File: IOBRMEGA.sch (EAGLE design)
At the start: 21 parts, among them J1 Digital_0_7, J10 Power, J2 Analog, J3 Digital_8_13, J4 Analog, J5 Digital_0_7, J6 Digital_22_36, J7 Digital_23_37, J8 Digital_38_52, J9 Digital_39_53

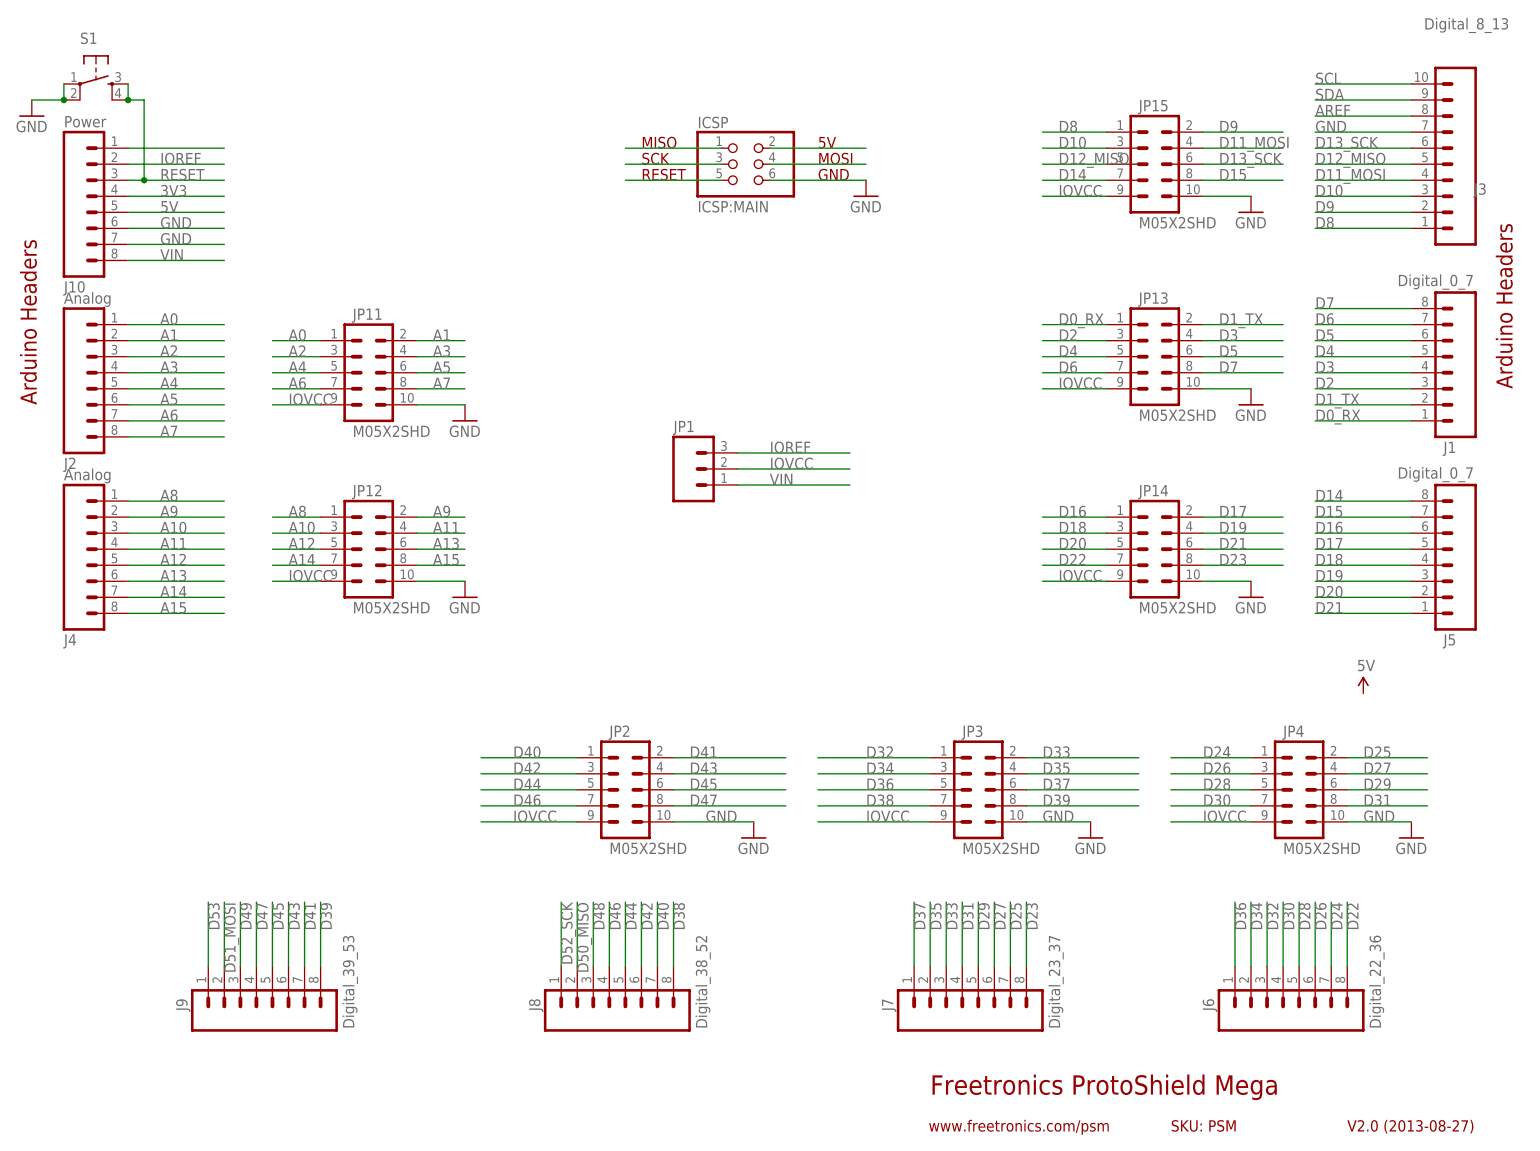
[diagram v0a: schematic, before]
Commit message: Expanded headers to 2x6 to include IOREF and RESET for v2.0 release
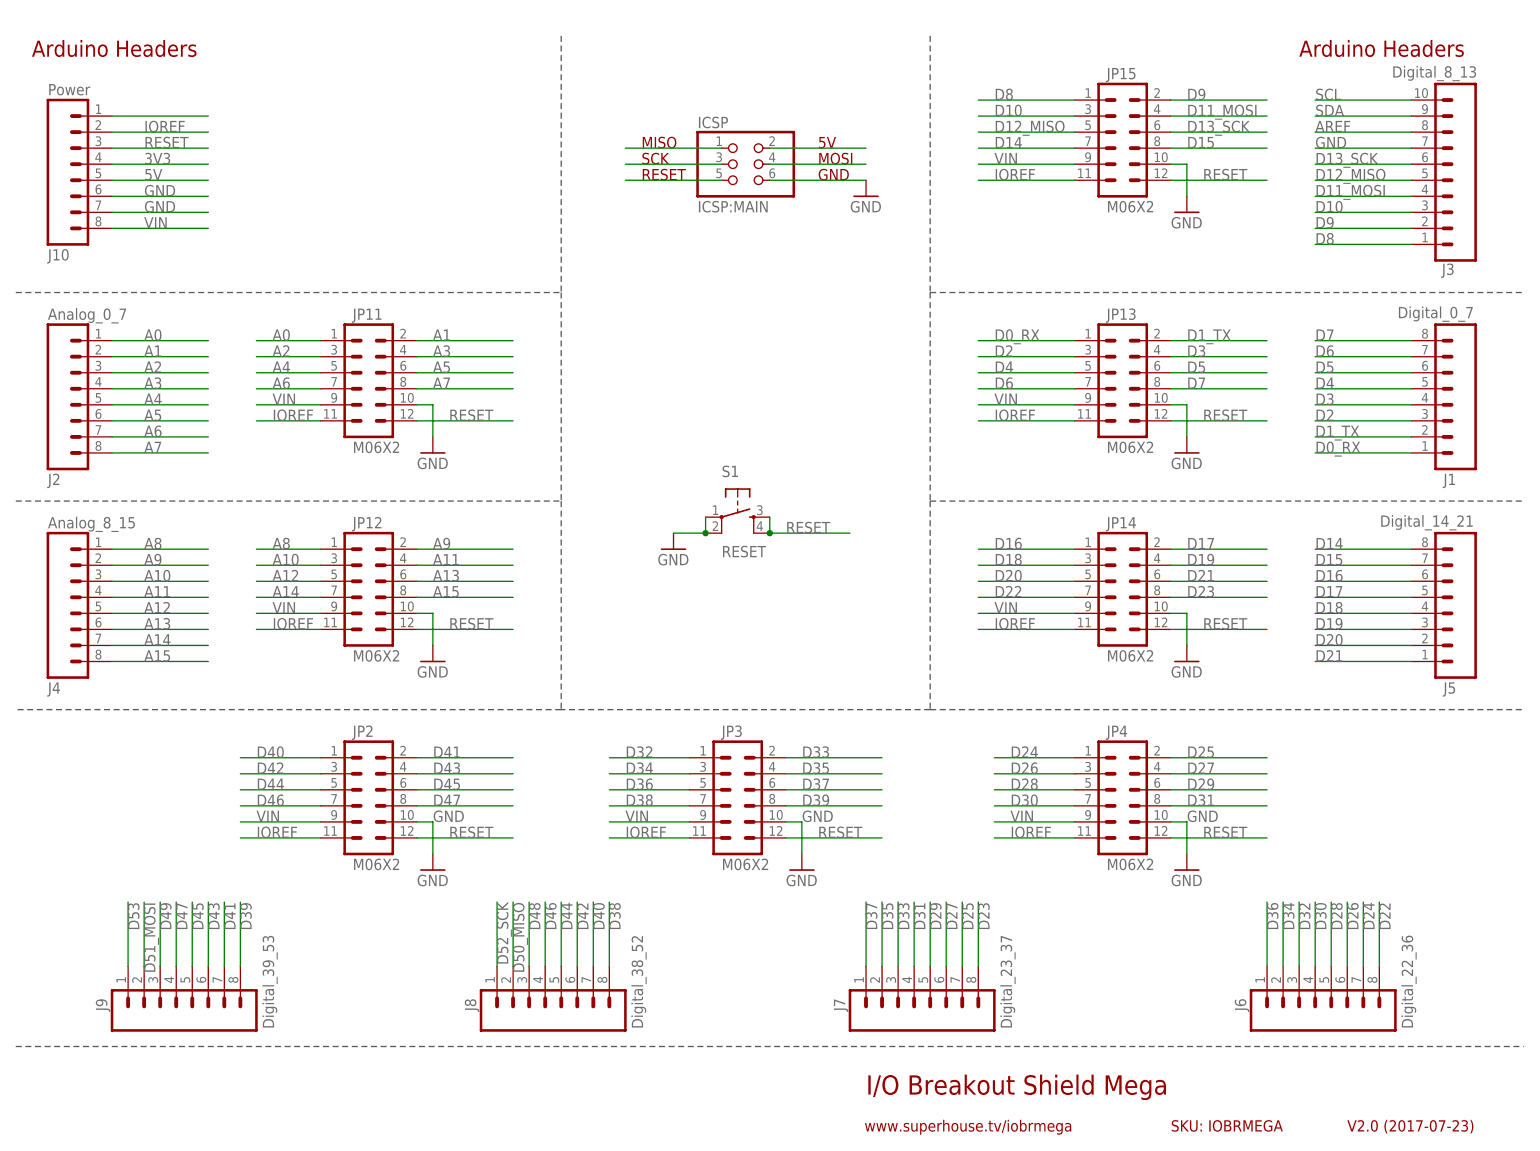
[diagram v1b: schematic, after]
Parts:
- removed JP1: (no value), freetronics-master-v1.1:M03PTH
- J2: value Analog -> Analog_0_7
- J4: value Analog -> Analog_8_15
- J5: value Digital_0_7 -> Digital_14_21
- JP11, JP12, JP13, JP14, JP15, JP2, JP3, JP4: value M05X2SHD -> M06X2; device freetronics-original:M05X2SHD -> freetronics-jon:M06X2
- S1: value (none) -> RESET
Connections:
- removed net IOVCC: JP1.2, JP11.9, JP12.9, JP13.9, JP14.9, JP15.9, JP2.9, JP3.9, JP4.9
- net IOREF: now also JP11.11, JP12.11, JP13.11, JP14.11, JP15.11, JP2.11, JP3.11, JP4.11; no longer JP1.3
- net RESET: now also JP11.12, JP12.12, JP13.12, JP14.12, JP15.12, JP2.12, JP3.12, JP4.12
- net VIN: now also JP11.9, JP12.9, JP13.9, JP14.9, JP15.9, JP2.9, JP3.9, JP4.9; no longer JP1.1
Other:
- note added: "I/O Breakout Shield Mega"
- note added: "SKU: IOBRMEGA"
- note added: "V2.0 (2017-07-23)"
- note added: "www.superhouse.tv/iobrmega"
- note removed: "Freetronics ProtoShield Mega"
- note removed: "SKU: PSM"
- note removed: "V2.0 (2013-08-27)"
- note removed: "www.freetronics.com/psm"
- moved on the sheet: J1, J10, J2, J3, J4, J5, J6, J7, J8, J9, S1

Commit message: Part swap to SuperHouse library to add 3D models
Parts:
- JP11, JP12, JP13, JP14, JP15, JP2, JP3, JP4: value M06X2 -> M06X2-SHROUDED; device freetronics-jon:M06X2 -> SuperHouse-Connectors:M06X2-SHROUDED
- S1: device freetronics-master-v1:TAC_SWITCHPTH -> SuperHouse-Switches:TAC_SWITCH-PTH-6

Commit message: Updated for v2.1 release
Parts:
- J1, J5, J6, J7, J8, J9: device freetronics:M08 -> SuperHouse-Connectors:M08-PIN-BELOW
- J10, J2, J4: device freetronics-master-v1:M08 -> SuperHouse-Connectors:M08-PIN-BELOW
- J3: device freetronics-original:M100.1 -> SuperHouse-Connectors:M10-PIN-BELOW
- renumbered ICSP to J19, JP11 to J11, JP12 to J12, JP13 to J17, JP14 to J16, JP15 to J18, JP2 to J13, JP3 to J14, JP4 to J15
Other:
- note added: "V2.1 (2019-10-25)"
- note removed: "V2.0 (2017-07-23)"

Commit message: Final tweaks for v2.1 release
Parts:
- J11, J12, J13, J14, J15, J16, J17, J18: value M06X2-SHROUDED -> M02X6-SHROUDED; device SuperHouse-Connectors:M06X2-SHROUDED -> SuperHouse-Connectors:M02X6-SHROUDED
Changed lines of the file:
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@@
 <part name="J8" library="SuperHouse-Connectors" library_urn="urn:adsk.eagle:library:11765989" deviceset="M08" device="-PIN-BELOW" package3d_urn="urn:adsk.eagle:package:14732715/3" value="Digital_38_52"/>
 <part name="J9" library="SuperHouse-Connectors" library_urn="urn:adsk.eagle:library:11765989" deviceset="M08" device="-PIN-BELOW" package3d_urn="urn:adsk.eagle:package:14732715/3" value="Digital_39_53"/>
-<part name="J19" library="pinhead" deviceset="PINHD-2X3" device="" value="ICSP:MAIN"/>
+<part name="J19" library="pinhead" library_urn="urn:adsk.eagle:library:325" deviceset="PINHD-2X3" device="" package3d_urn="urn:adsk.eagle:package:22462/2" value="ICSP:MAIN"/>
 <part name="J10" library="SuperHouse-Connectors" library_urn="urn:adsk.eagle:library:11765989" deviceset="M08" device="-PIN-BELOW" package3d_urn="urn:adsk.eagle:package:14732715/3" value="Power"/>
-<part name="J11" library="SuperHouse-Connectors" library_urn="urn:adsk.eagle:library:11765989" deviceset="M06X2" device="-SHROUDED" package3d_urn="urn:adsk.eagle:package:11976015/2"/>
-<part name="J12" library="SuperHouse-Connectors" library_urn="urn:adsk.eagle:library:11765989" deviceset="M06X2" device="-SHROUDED" package3d_urn="urn:adsk.eagle:package:11976015/2"/>
-<part name="J17" library="SuperHouse-Connectors" library_urn="urn:adsk.eagle:library:11765989" deviceset="M06X2" device="-SHROUDED" package3d_urn="urn:adsk.eagle:package:11976015/2"/>
-<part name="J16" library="SuperHouse-Connectors" library_urn="urn:adsk.eagle:library:11765989" deviceset="M06X2" device="-SHROUDED" package3d_urn="urn:adsk.eagle:package:11976015/2"/>
-<part name="J18" library="SuperHouse-Connectors" library_urn="urn:adsk.eagle:library:11765989" deviceset="M06X2" device="-SHROUDED" package3d_urn="urn:adsk.eagle:package:11976015/2"/>
-<part name="J13" library="SuperHouse-Connectors" library_urn="urn:adsk.eagle:library:11765989" deviceset="M06X2" device="-SHROUDED" package3d_urn="urn:adsk.eagle:package:11976015/2"/>
-<part name="J14" library="SuperHouse-Connectors" library_urn="urn:adsk.eagle:library:11765989" deviceset="M06X2" device="-SHROUDED" package3d_urn="urn:adsk.eagle:package:11976015/2"/>
-<part name="J15" library="SuperHouse-Connectors" library_urn="urn:adsk.eagle:library:11765989" deviceset="M06X2" device="-SHROUDED" package3d_urn="urn:adsk.eagle:package:11976015/2"/>
+<part name="J11" library="SuperHouse-Connectors" library_urn="urn:adsk.eagle:library:11765989" deviceset="M02X6" device="-SHROUDED" package3d_urn="urn:adsk.eagle:package:11976015/5"/>
+<part name="J12" library="SuperHouse-Connectors" library_urn="urn:adsk.eagle:library:11765989" deviceset="M02X6" device="-SHROUDED" package3d_urn="urn:adsk.eagle:package:11976015/5"/>
+<part name="J17" library="SuperHouse-Connectors" library_urn="urn:adsk.eagle:library:11765989" deviceset="M02X6" device="-SHROUDED" package3d_urn="urn:adsk.eagle:package:11976015/5"/>
+<part name="J16" library="SuperHouse-Connectors" library_urn="urn:adsk.eagle:library:11765989" deviceset="M02X6" device="-SHROUDED" package3d_urn="urn:adsk.eagle:package:11976015/5"/>
+<part name="J18" library="SuperHouse-Connectors" library_urn="urn:adsk.eagle:library:11765989" deviceset="M02X6" device="-SHROUDED" package3d_urn="urn:adsk.eagle:package:11976015/5"/>
+<part name="J13" library="SuperHouse-Connectors" library_urn="urn:adsk.eagle:library:11765989" deviceset="M02X6" device="-SHROUDED" package3d_urn="urn:adsk.eagle:package:11976015/5"/>
+<part name="J14" library="SuperHouse-Connectors" library_urn="urn:adsk.eagle:library:11765989" deviceset="M02X6" device="-SHROUDED" package3d_urn="urn:adsk.eagle:package:11976015/5"/>
+<part name="J15" library="SuperHouse-Connectors" library_urn="urn:adsk.eagle:library:11765989" deviceset="M02X6" device="-SHROUDED" package3d_urn="urn:adsk.eagle:package:11976015/5"/>
 <part name="GND1" library="freetronics-original" deviceset="GND" device=""/>
 <part name="GND2" library="freetronics-original" deviceset="GND" device=""/>
